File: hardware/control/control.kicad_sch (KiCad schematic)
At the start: 58 parts, among them J1 Conn_01x05_Male, J2 CANPWR, J3 CANGND, J4 RJ45, J5 RJ45, J6 Conn_02x03_Odd_Even, J7 DCDC-PWM, J8 DCDC-MEASURES, J9 display, Q1 BSS123, SW1 next, SW2 select, U1 2.048V, U2 AP63200WU, U3 PIC18F27Q84, U4 TLE9250VSJXUMA1, Y1 10Mhz

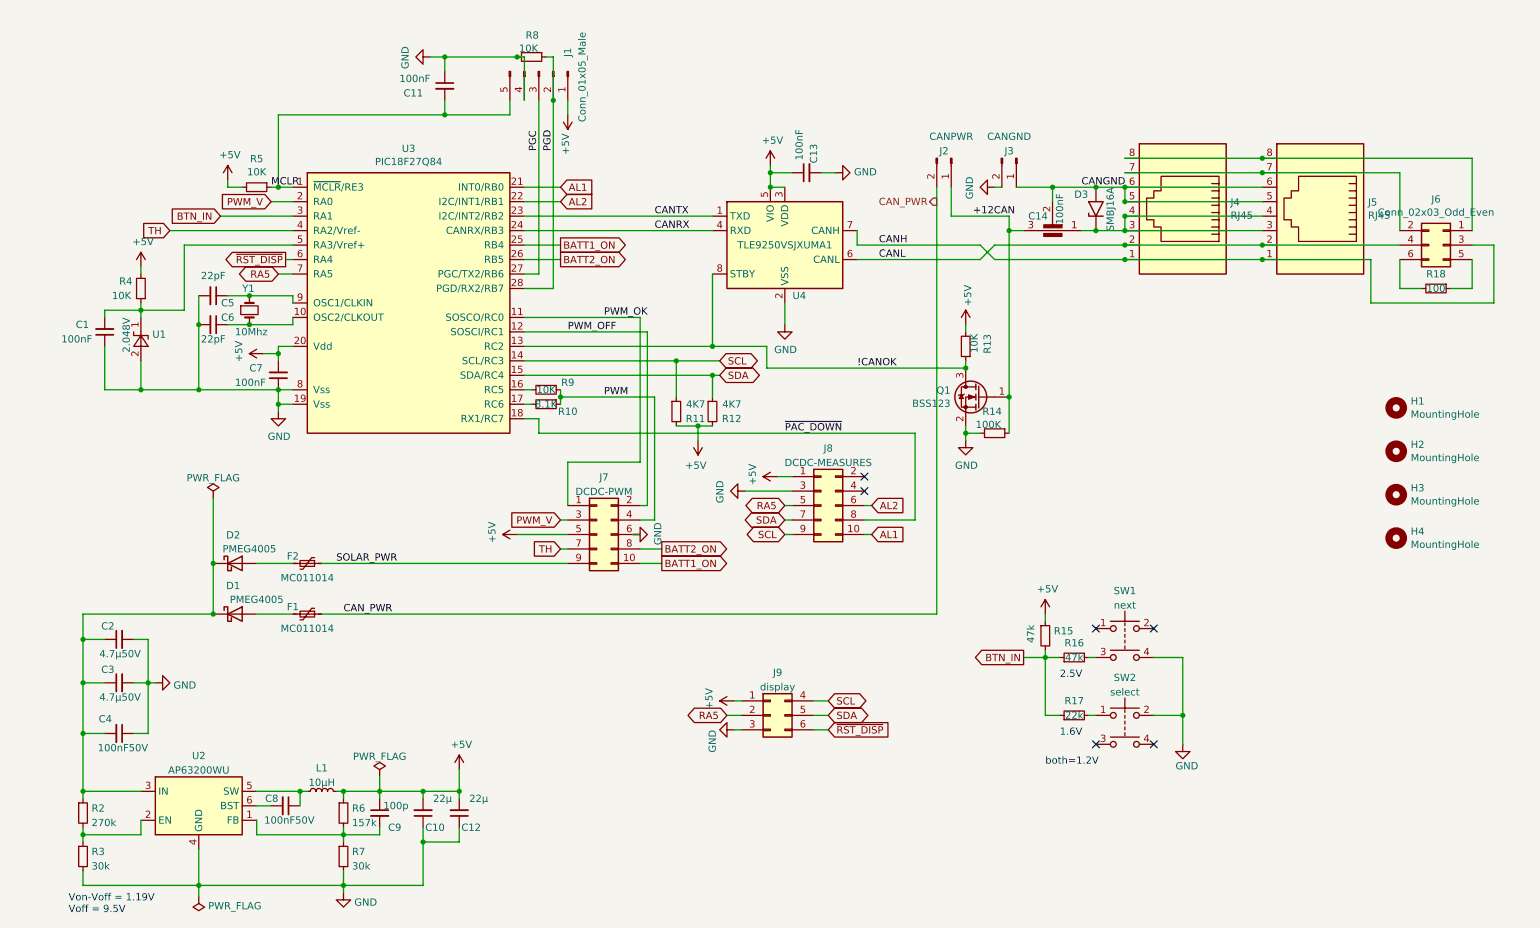
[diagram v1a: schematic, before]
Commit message: On second though, the pac1953  won't be fast enough for the PWM regulation loop. So add a resistor divider routed to RA5 to get the solar voltage from the PIC18's ADC.
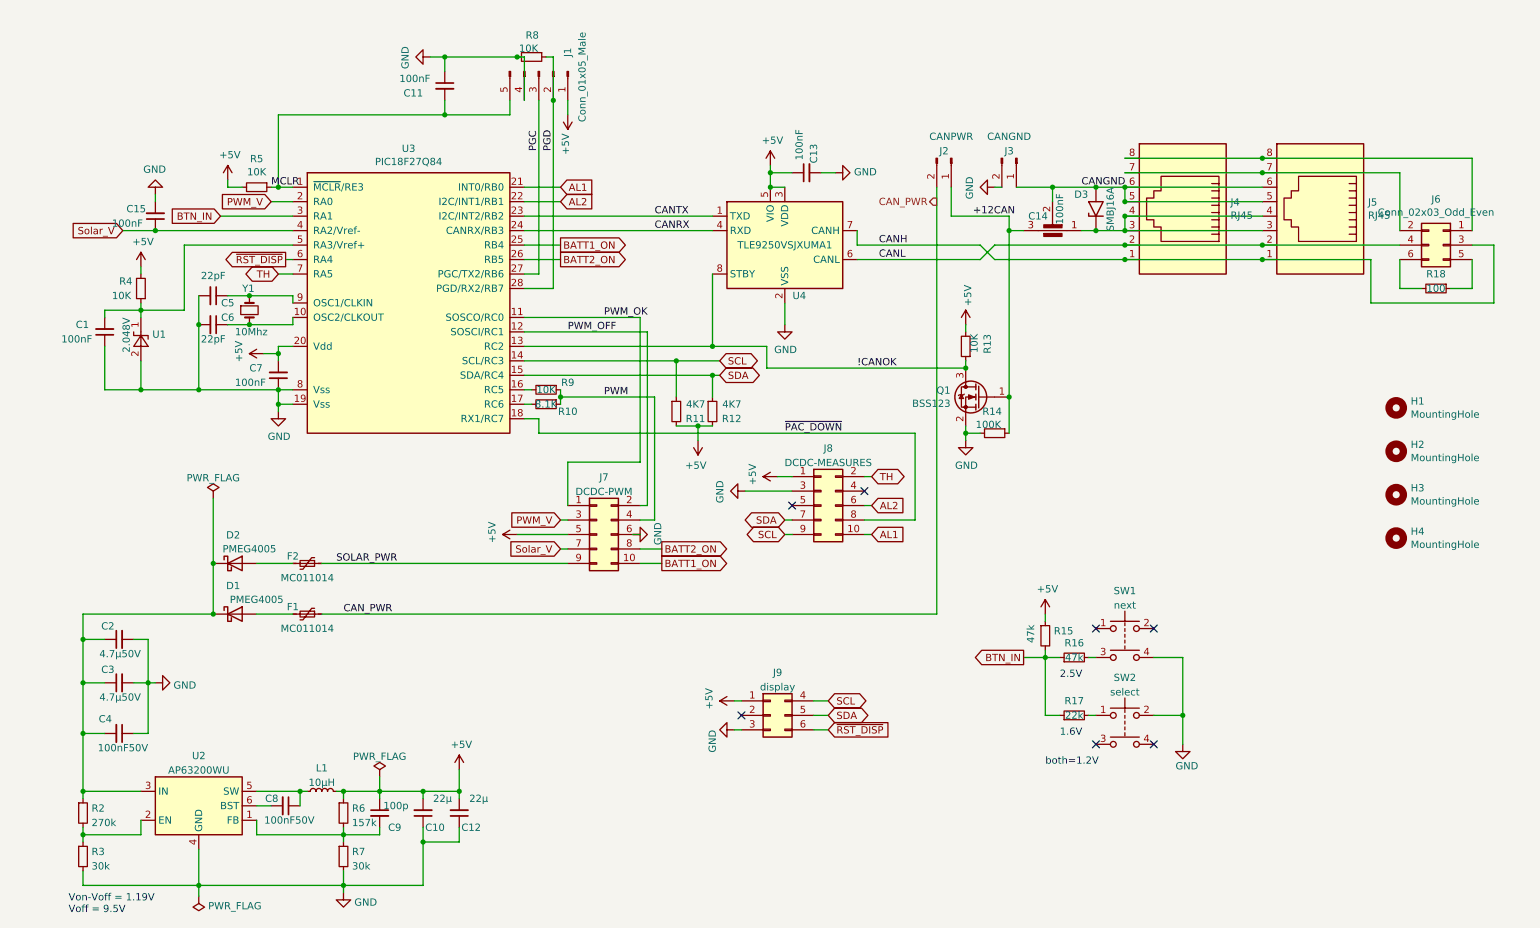
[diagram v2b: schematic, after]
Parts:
- added C15: 100nF, Capacitor_SMD:C_0603_1608Metric_Pad1.08x0.95mm_HandSolder, symbol Device:C_Small
- R12: footprint Resistor_THT:R_Axial_DIN0309_L9.0mm_D3.2mm_P12.70mm_Horizontal -> Resistor_THT:R_Axial_DIN0207_L6.3mm_D2.5mm_P10.16mm_Horizontal
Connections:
- net GND: now also C15.2
- net TH: now also J8.2 (Pin_2), U3.7 (RA5); no longer J7.7 (Pin_7), U3.4 (RA2/Vref-)
- removed net RA5: J8.5 (Pin_5), J9.2 (Pin_2), U3.7 (RA5)
- new net Solar_V: C15.1, J7.7 (Pin_7), U3.4 (RA2/Vref-)
- no-connect marks 6 -> 7
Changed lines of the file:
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@@
   (junction (at 107.95 86.36) (diameter 0) (color 0 0 0 0)
+  )
+  (junction (at 36.83 57.15) (diameter 0) (color 0 0 0 0)
   )
   (junction (at 53.34 68.58) (diameter 0) (color 0 0 0 0)
@@
   (no_connect (at 201.93 127))
   (no_connect (at 161.29 102.87))
-  (no_connect (at 161.29 100.33))
+  (no_connect (at 148.59 105.41))
+  (no_connect (at 139.7 142.24))
   (wire (pts (xy 101.6 80.01) (xy 128.27 80.01))
     (stroke (width 0) (type default) (color 0 0 0 0))
@@
     (stroke (width 0) (type default) (color 0 0 0 0))
   )
-  (wire (pts (xy 39.37 57.15) (xy 60.96 57.15))
+  (wire (pts (xy 31.115 57.15) (xy 36.83 57.15))
     (stroke (width 0) (type default) (color 0 0 0 0))
   )
@@
     (stroke (width 0) (type default) (color 0 0 0 0))
   )
-  (wire (pts (xy 137.16 142.24) (xy 139.7 142.24))
-    (stroke (width 0) (type default) (color 0 0 0 0))
-  )
   (wire (pts (xy 90.17 155.575) (xy 90.17 156.845))
     (stroke (width 0) (type default) (color 0 0 0 0))
@@
     (stroke (width 0) (type default) (color 0 0 0 0))
   )
-  (wire (pts (xy 147.32 105.41) (xy 148.59 105.41))
-    (stroke (width 0) (type default) (color 0 0 0 0))
-  )
   (wire (pts (xy 207.01 54.61) (xy 231.14 54.61))
     (stroke (width 0) (type default) (color 0 0 0 0))
@@
     (stroke (width 0) (type default) (color 0 0 0 0))
   )
+  (wire (pts (xy 161.29 100.33) (xy 162.56 100.33))
+    (stroke (width 0) (type default) (color 0 0 0 0))
+  )
   (wire (pts (xy 187.96 49.53) (xy 194.31 49.53))
     (stroke (width 0) (type default) (color 0 0 0 0))
@@
     (stroke (width 0) (type default) (color 0 0 0 0))
   )
+  (wire (pts (xy 36.83 57.15) (xy 60.96 57.15))
+    (stroke (width 0) (type default) (color 0 0 0 0))
+  )
   (wire (pts (xy 132.08 93.98) (xy 132.08 91.44))
     (stroke (width 0) (type default) (color 0 0 0 0))
@@
   )
   (wire (pts (xy 144.78 45.72) (xy 144.78 46.99))
+    (stroke (width 0) (type default) (color 0 0 0 0))
+  )
+  (wire (pts (xy 36.83 50.8) (xy 36.83 52.07))
     (stroke (width 0) (type default) (color 0 0 0 0))
   )
@@
     )
   )
-  (global_label "RA5" (shape tri_state) (at 58.42 64.77 180) (fields_autoplaced)
+  (global_label "TH" (shape tri_state) (at 58.42 64.77 180) (fields_autoplaced)
     (effects (font (size 1.27 1.27)) (justify right))
-    (property "Intersheet References" "${INTERSHEET_REFS}" (id 0) (at 52.4388 64.6906 0)
+    (property "Intersheet References" "${INTERSHEET_REFS}" (id 0) (at 53.7088 64.6906 0)
       (effects (font (size 1.27 1.27)) (justify right) hide)
     )
@@
     )
   )
-  (global_label "RA5" (shape tri_state) (at 137.16 142.24 180) (fields_autoplaced)
-    (effects (font (size 1.27 1.27)) (justify right))
-    (property "Intersheet References" "${INTERSHEET_REFS}" (id 0) (at 131.1788 142.1606 0)
-      (effects (font (size 1.27 1.27)) (justify right) hide)
-    )
-  )
   (global_label "AL2" (shape input) (at 162.56 105.41 0) (fields_autoplaced)
     (effects (font (size 1.27 1.27)) (justify left))
@@
     )
   )
-  (global_label "TH" (shape input) (at 39.37 57.15 180) (fields_autoplaced)
+  (global_label "Solar_V" (shape input) (at 31.115 57.15 180) (fields_autoplaced)
     (effects (font (size 1.27 1.27)) (justify right))
-    (property "Intersheet References" "${INTERSHEET_REFS}" (id 0) (at 34.6588 57.0706 0)
+    (property "Intersheet References" "${INTERSHEET_REFS}" (id 0) (at 21.6867 57.0706 0)
       (effects (font (size 1.27 1.27)) (justify right) hide)
     )
@@
     )
   )
-  (global_label "TH" (shape input) (at 107.95 113.03 180) (fields_autoplaced)
+  (global_label "Solar_V" (shape input) (at 107.95 113.03 180) (fields_autoplaced)
     (effects (font (size 1.27 1.27)) (justify right))
-    (property "Intersheet References" "${INTERSHEET_REFS}" (id 0) (at 103.2388 112.9506 0)
+    (property "Intersheet References" "${INTERSHEET_REFS}" (id 0) (at 98.5217 112.9506 0)
       (effects (font (size 1.27 1.27)) (justify right) hide)
     )
   )
-  (global_label "RA5" (shape tri_state) (at 147.32 105.41 180) (fields_autoplaced)
-    (effects (font (size 1.27 1.27)) (justify right))
-    (property "Intersheet References" "${INTERSHEET_REFS}" (id 0) (at 141.3388 105.3306 0)
-      (effects (font (size 1.27 1.27)) (justify right) hide)
+  (global_label "TH" (shape tri_state) (at 162.56 100.33 0) (fields_autoplaced)
+    (effects (font (size 1.27 1.27)) (justify left))
+    (property "Intersheet References" "${INTERSHEET_REFS}" (id 0) (at 167.2712 100.4094 0)
+      (effects (font (size 1.27 1.27)) (justify left) hide)
     )
   )
@@
       (effects (font (size 1.27 1.27)) hide)
     )
+  )
+  (symbol (lib_id "Device:C_Small") (at 36.83 54.61 180) (unit 1)
+    (in_bom yes) (on_board yes)
+    (property "Reference" "C15" (id 0) (at 31.75 53.34 0)
+      (effects (font (size 1.27 1.27)) (justify right))
+    )
+    (property "Value" "100nF" (id 1) (at 29.21 55.88 0)
+      (effects (font (size 1.27 1.27)) (justify right))
+    )
+    (property "Footprint" "Capacitor_SMD:C_0603_1608Metric_Pad1.08x0.95mm_HandSolder" (id 2) (at 36.83 54.61 0)
+      (effects (font (size 1.27 1.27)) hide)
+    )
+    (property "Datasheet" "~" (id 3) (at 36.83 54.61 0)
+      (effects (font (size 1.27 1.27)) hide)
+    )
+    (property "P/N" "MC0603B104K250CT" (id 4) (at 36.83 54.61 0)
+      (effects (font (size 1.27 1.27)) hide)
+    )
+    (pin "1")
+    (pin "2")
   )
   (symbol (lib_id "power:+5V") (at 138.43 139.7 90) (unit 1)
@@
       (effects (font (size 1.27 1.27)) (justify right))
     )
-    (property "Footprint" "Resistor_THT:R_Axial_DIN0309_L9.0mm_D3.2mm_P12.70mm_Horizontal" (id 2) (at 134.62 88.9 0)
+    (property "Footprint" "Resistor_THT:R_Axial_DIN0207_L6.3mm_D2.5mm_P10.16mm_Horizontal" (id 2) (at 134.62 88.9 0)
       (effects (font (size 1.27 1.27)) hide)
     )
@@
     (pin "2")
   )
+  (symbol (lib_id "power:GND") (at 36.83 50.8 180) (unit 1)
+    (in_bom yes) (on_board yes)
+    (property "Reference" "#PWR0105" (id 0) (at 36.83 44.45 0)
+      (effects (font (size 1.27 1.27)) hide)
+    )
+    (property "Value" "GND" (id 1) (at 36.703 46.4058 0))
+    (property "Footprint" "" (id 2) (at 36.83 50.8 0)
+      (effects (font (size 1.27 1.27)) hide)
+    )
+    (property "Datasheet" "" (id 3) (at 36.83 50.8 0)
+      (effects (font (size 1.27 1.27)) hide)
+    )
+    (pin "1")
+  )
   (symbol (lib_id "Device:C_Small") (at 151.13 46.99 90) (unit 1)
     (in_bom yes) (on_board yes)
@@
       (reference "#PWR0104") (unit 1) (value "GND") (footprint "")
     )
+    (path "/fceb03cc-d7a5-4a17-a0bd-f25ee2035965"
+      (reference "#PWR0105") (unit 1) (value "GND") (footprint "")
+    )
     (path "/0c0222ff-2875-415e-9bf8-78a11b090087"
       (reference "C1") (unit 1) (value "100nF") (footprint "Capacitor_SMD:C_0603_1608Metric_Pad1.08x0.95mm_HandSolder")
@@
       (reference "C14") (unit 1) (value "100nF") (footprint "local:C_filter_0805")
     )
+    (path "/012b97ad-a232-4ccb-8205-1ebee8f32925"
+      (reference "C15") (unit 1) (value "100nF") (footprint "Capacitor_SMD:C_0603_1608Metric_Pad1.08x0.95mm_HandSolder")
+    )
     (path "/0fe60029-f7e3-4007-a3d9-2206cadbe88f"
       (reference "D1") (unit 1) (value "PMEG4005") (footprint "Diode_SMD:D_SOD-123")
@@
     )
     (path "/51f0f55e-83ce-4497-b09e-c6e1e4b03e19"
-      (reference "R12") (unit 1) (value "4K7") (footprint "Resistor_THT:R_Axial_DIN0309_L9.0mm_D3.2mm_P12.70mm_Horizontal")
+      (reference "R12") (unit 1) (value "4K7") (footprint "Resistor_THT:R_Axial_DIN0207_L6.3mm_D2.5mm_P10.16mm_Horizontal")
     )
     (path "/9cd13088-9280-42ff-88e7-8341e2a75837"

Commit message: Re-annotate schematics
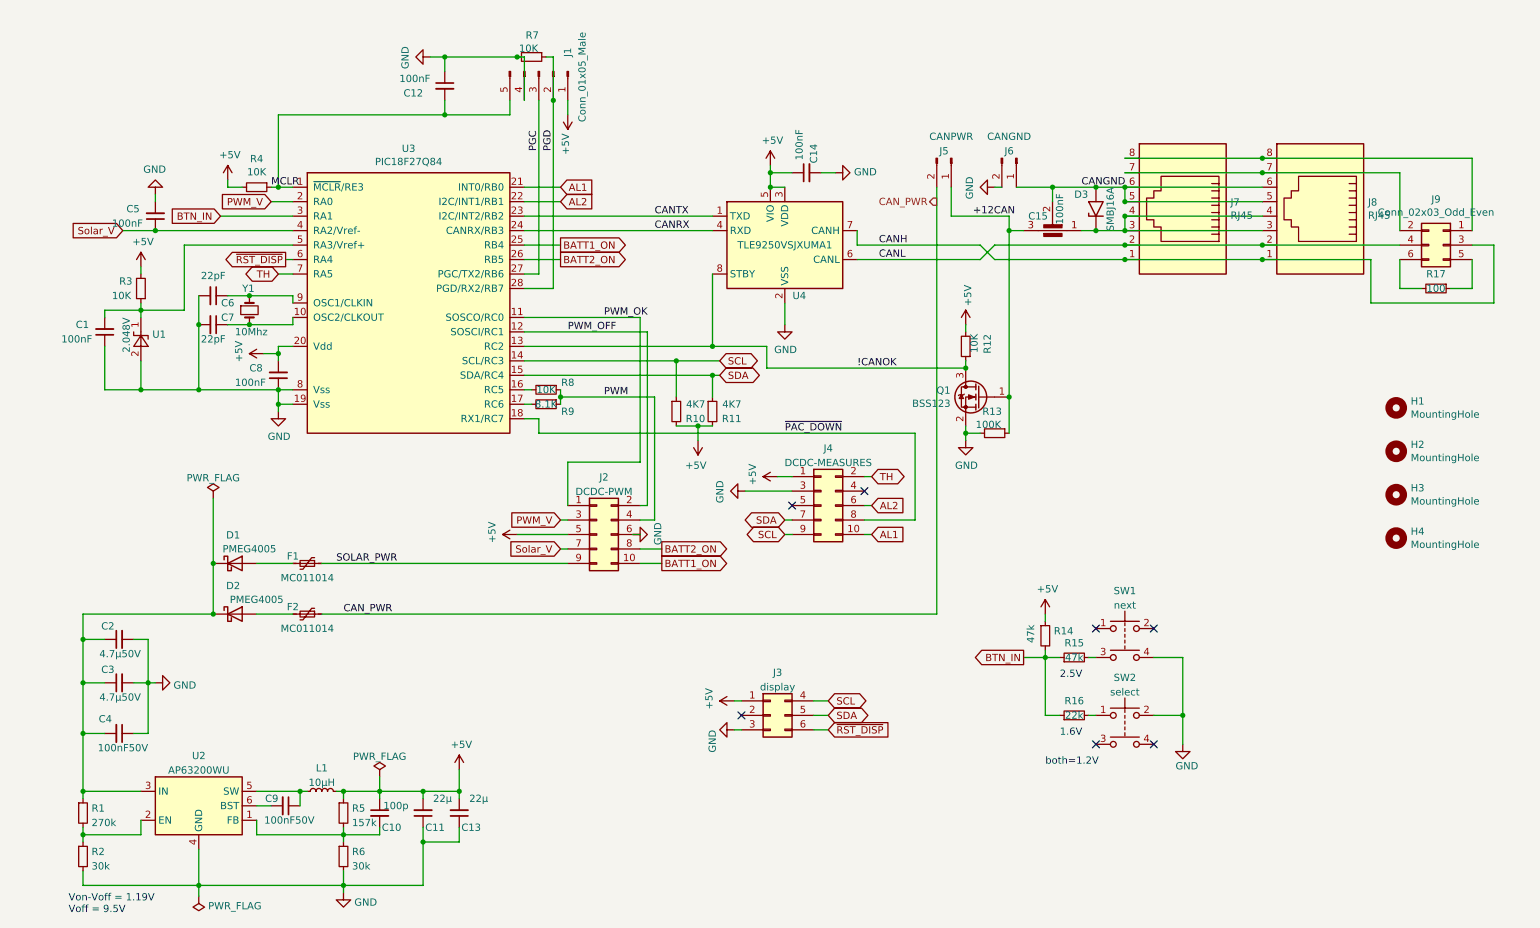
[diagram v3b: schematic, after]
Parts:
- renumbered C9 to C10, C10 to C11, C11 to C12, C12 to C13, C13 to C14, C14 to C15, C15 to C5, C5 to C6, C6 to C7, C7 to C8, C8 to C9, D2 to D1, D1 to D2, F2 to F1, F1 to F2, J7 to J2, J9 to J3, J8 to J4, J2 to J5, J3 to J6, J4 to J7, J5 to J8, J6 to J9, R2 to R1, R11 to R10, R12 to R11, R13 to R12, R14 to R13, R15 to R14, R16 to R15, R17 to R16, R18 to R17, R3 to R2, R4 to R3, R5 to R4, R6 to R5, R7 to R6, R8 to R7, R9 to R8, R10 to R9
